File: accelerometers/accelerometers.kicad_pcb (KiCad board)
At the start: 2 copper layers, 49.2 x 41.8 mm, 84 parts, among them J1 USB-Mini, J2 HEADER_1X6, M1 MNT-3MM, M2 MNT-3MM, M3 MNT-3MM, M4 MNT-3MM, Q1 MOSFET-N, Q2 MOSFET-N, Q3 MOSFET-N, Q4 MOSFET-N, Q5 MOSFET-N, Q6 MOSFET-N, U1 KXTJ3-1057, U2 TD230XQ, U3 LIS2HH12, U4 Temp_SOT23-3, U5 PIC16F1829_SOIC

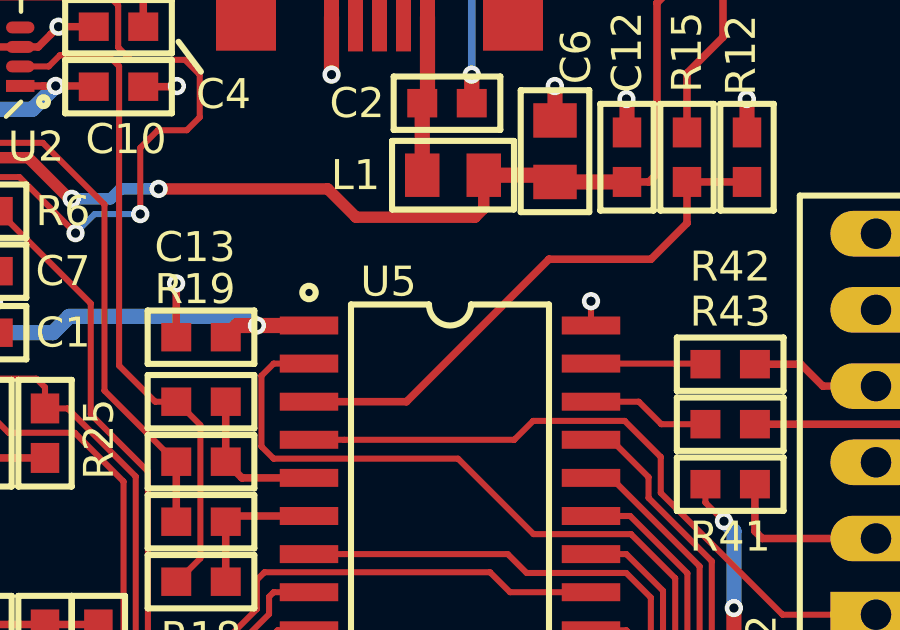
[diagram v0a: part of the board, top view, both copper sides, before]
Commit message: Updating accelerometers to new kicad 7
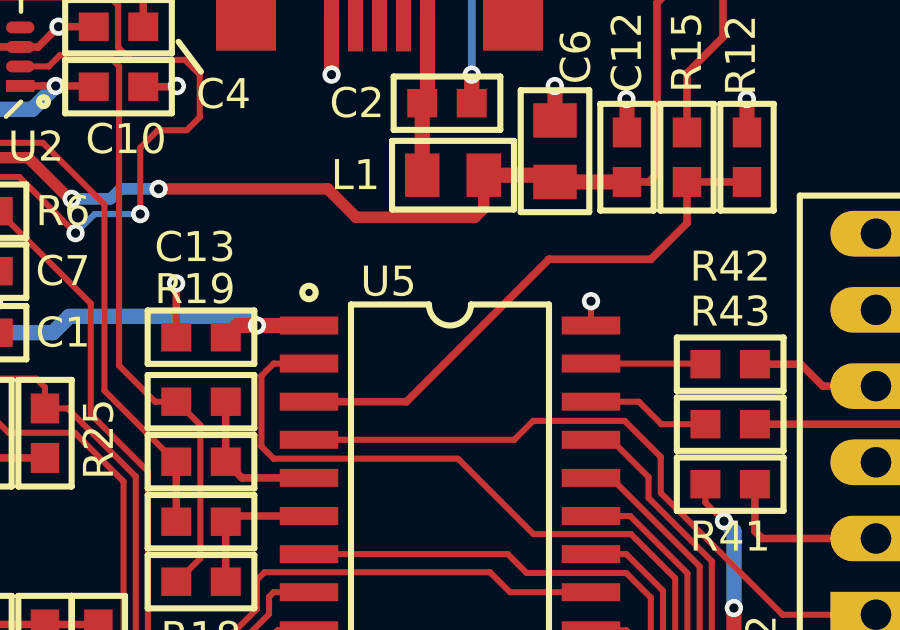
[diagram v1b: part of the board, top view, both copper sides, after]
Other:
- net class Default removed
